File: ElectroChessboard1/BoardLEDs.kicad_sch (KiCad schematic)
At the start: 35 parts, among them IC73 CD74HC154M96

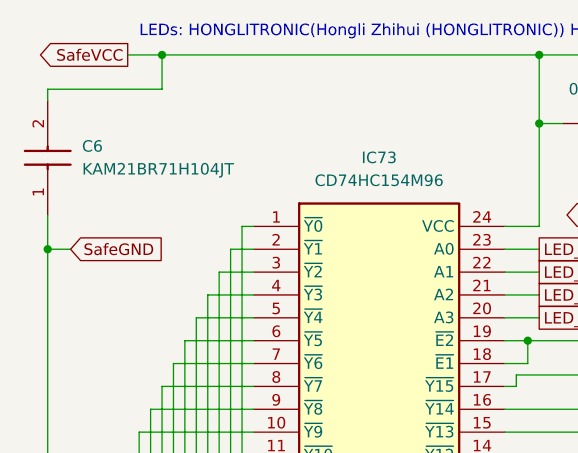
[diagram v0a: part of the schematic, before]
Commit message: Corrected footprints 1
Chosen footprints for JLCPCB
I may add USB insterface chip
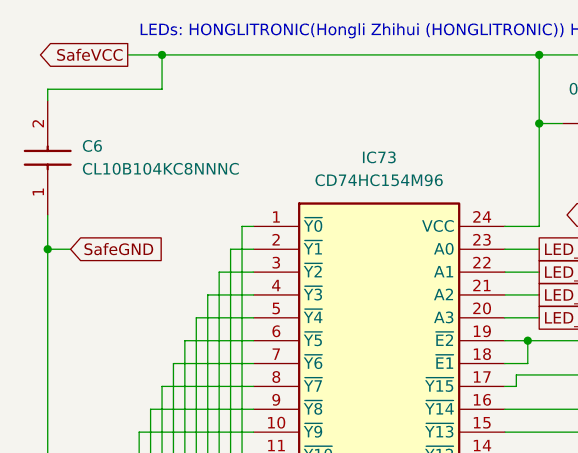
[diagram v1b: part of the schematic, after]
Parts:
- removed C6: KAM21BR71H104JT, CAPC2012X94N, symbol SamacSys_Parts:KAM21BR71H104JT
- added C6: CL10B104KC8NNNC, SamacSys_Parts:CAPC1608X90N, symbol SamacSys_Parts:CL10B104KC8NNNC
- IC73: footprint SOIC127P1030X265-24N -> SamacSys_Parts:SOIC127P1030X265-24N
- R10, R11, R12, R13, R14, R15, R16, R17, R18, R19, R2, R4, R5, R6, R7, R8, R9: footprint RESC1005X40N -> SamacSys_Parts:RESC1005X40N
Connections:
- net SafeGND: now also C6.1
- net SafeVCC: now also C6.2
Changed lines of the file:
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@@
 			)
 		)
-		(property "Footprint" "RESC1005X40N"
+		(property "Footprint" "SamacSys_Parts:RESC1005X40N"
 			(at 104.14 285.42 0)
 			(effects
@@
 			)
 		)
-		(property "Footprint" "RESC1005X40N"
+		(property "Footprint" "SamacSys_Parts:RESC1005X40N"
 			(at 104.14 193.98 0)
 			(effects
@@
 			)
 		)
-		(property "Footprint" "RESC1005X40N"
+		(property "Footprint" "SamacSys_Parts:RESC1005X40N"
 			(at 104.14 248.59 0)
 			(effects
@@
 			)
 		)
-		(property "Footprint" "RESC1005X40N"
+		(property "Footprint" "SamacSys_Parts:RESC1005X40N"
 			(at 104.14 166.04 0)
 			(effects
@@
 			)
 		)
-		(property "Footprint" "RESC1005X40N"
+		(property "Footprint" "SamacSys_Parts:RESC1005X40N"
 			(at 104.14 202.87 0)
 			(effects
@@
 	)
 	(symbol
+		(lib_id "SamacSys_Parts:CL10B104KC8NNNC")
+		(at 16.51 34.29 90)
+		(unit 1)
+		(exclude_from_sim no)
+		(in_bom yes)
+		(on_board yes)
+		(dnp no)
+		(fields_autoplaced yes)
+		(property "Reference" "C6"
+			(at 20.32 26.6699 90)
+			(effects
+				(font
+					(size 1.27 1.27)
+				)
+				(justify right)
+			)
+		)
+		(property "Value" "CL10B104KC8NNNC"
+			(at 20.32 29.2099 90)
+			(effects
+				(font
+					(size 1.27 1.27)
+				)
+				(justify right)
+			)
+		)
+		(property "Footprint" "SamacSys_Parts:CAPC1608X90N"
+			(at 112.7 25.4 0)
+			(effects
+				(font
+					(size 1.27 1.27)
+				)
+				(justify left top)
+				(hide yes)
+			)
+		)
+		(property "Datasheet" "https://datasheet.datasheetarchive.com/originals/distributors/DKDS-19/373511.pdf"
+			(at 212.7 25.4 0)
+			(effects
+				(font
+					(size 1.27 1.27)
+				)
+				(justify left top)
+				(hide yes)
+			)
+		)
+		(property "Description" "Samsung"
+			(at 16.51 34.29 0)
+			(effects
+				(font
+					(size 1.27 1.27)
+				)
+				(hide yes)
+			)
+		)
+		(property "Height" "0.9"
+			(at 412.7 25.4 0)
+			(effects
+				(font
+					(size 1.27 1.27)
+				)
+				(justify left top)
+				(hide yes)
+			)
+		)
+		(property "Mouser Part Number" "187-CL10B104KC8NNNC"
+			(at 512.7 25.4 0)
+			(effects
+				(font
+					(size 1.27 1.27)
+				)
+				(justify left top)
+				(hide yes)
+			)
+		)
+		(property "Mouser Price/Stock" "https://www.mouser.co.uk/ProductDetail/Samsung-Electro-Mechanics/CL10B104KC8NNNC?qs=%2FukktrhNKsY5bKXvqblW4Q%3D%3D"
+			(at 612.7 25.4 0)
+			(effects
+				(font
+					(size 1.27 1.27)
+				)
+				(justify left top)
+				(hide yes)
+			)
+		)
+		(property "Manufacturer_Name" "SAMSUNG"
+			(at 712.7 25.4 0)
+			(effects
+				(font
+					(size 1.27 1.27)
+				)
+				(justify left top)
+				(hide yes)
+			)
+		)
+		(property "Manufacturer_Part_Number" "CL10B104KC8NNNC"
+			(at 812.7 25.4 0)
+			(effects
+				(font
+					(size 1.27 1.27)
+				)
+				(justify left top)
+				(hide yes)
+			)
+		)
+		(pin "2"
+		)
+		(pin "1"
+		)
+		(instances
+			(project "ElectroChessboard1"
+				(path "/b40c7e57-cfb3-41c6-81be-f22d082b0927/7327273e-7754-4727-8b52-bb7f62babc74"
+					(reference "C6")
+					(unit 1)
+				)
+			)
+		)
+	)
+	(symbol
 		(lib_id "Device:LED")
 		(at 83.82 143.51 0)
@@
 			)
 		)
-		(property "Footprint" "RESC1005X40N"
+		(property "Footprint" "SamacSys_Parts:RESC1005X40N"
 			(at 104.14 185.09 0)
 			(effects
@@
 			)
 		)
-		(property "Footprint" "SOIC127P1030X265-24N"
+		(property "Footprint" "SamacSys_Parts:SOIC127P1030X265-24N"
 			(at 63.5 130.48 0)
 			(effects
@@
 			)
 		)
-		(property "Footprint" "RESC1005X40N"
+		(property "Footprint" "SamacSys_Parts:RESC1005X40N"
 			(at 104.14 258.75 0)
 			(effects
@@
 			)
 		)
-		(property "Footprint" "RESC1005X40N"
+		(property "Footprint" "SamacSys_Parts:RESC1005X40N"
 			(at 104.14 239.7 0)
 			(effects
@@
 			)
 		)
-		(property "Footprint" "RESC1005X40N"
+		(property "Footprint" "SamacSys_Parts:RESC1005X40N"
 			(at 104.14 276.53 0)
 			(effects
@@
 			)
 		)
-		(property "Footprint" "RESC1005X40N"
+		(property "Footprint" "SamacSys_Parts:RESC1005X40N"
 			(at 104.14 211.76 0)
 			(effects
@@
 			)
 		)
-		(property "Footprint" "RESC1005X40N"
+		(property "Footprint" "SamacSys_Parts:RESC1005X40N"
 			(at 104.14 221.92 0)
 			(effects
@@
 			)
 		)
-		(property "Footprint" "RESC1005X40N"
+		(property "Footprint" "SamacSys_Parts:RESC1005X40N"
 			(at 104.14 230.81 0)
 			(effects
@@
 			)
 		)
-		(property "Footprint" "RESC1005X40N"
+		(property "Footprint" "SamacSys_Parts:RESC1005X40N"
 			(at 104.14 157.15 0)
 			(effects
@@
 			)
 		)
-		(property "Footprint" "RESC1005X40N"
+		(property "Footprint" "SamacSys_Parts:RESC1005X40N"
 			(at 104.14 267.64 0)
 			(effects
@@
 			)
 		)
-		(property "Footprint" "RESC1005X40N"
+		(property "Footprint" "SamacSys_Parts:RESC1005X40N"
 			(at 104.14 174.93 0)
 			(effects
@@
 	)
 	(symbol
-		(lib_id "SamacSys_Parts:KAM21BR71H104JT")
-		(at 16.51 34.29 90)
-		(unit 1)
-		(exclude_from_sim no)
-		(in_bom yes)
-		(on_board yes)
-		(dnp no)
-		(fields_autoplaced yes)
-		(property "Reference" "C6"
-			(at 20.32 26.6699 90)
-			(effects
-				(font
-					(size 1.27 1.27)
-				)
-				(justify right)
-			)
-		)
-		(property "Value" "KAM21BR71H104JT"
-			(at 20.32 29.2099 90)
-			(effects
-				(font
-					(size 1.27 1.27)
-				)
-				(justify right)
-			)
-		)
-		(property "Footprint" "CAPC2012X94N"
-			(at 112.7 25.4 0)
-			(effects
-				(font
-					(size 1.27 1.27)
-				)
-				(justify left top)
-				(hide yes)
-			)
-		)
-		(property "Datasheet" "https://spicat.kyocera-avx.com/product/mlcc/chartview/KAM21BR71H104JT/DataSheet/X7R"
-			(at 212.7 25.4 0)
-			(effects
-				(font
-					(size 1.27 1.27)
-				)
-				(justify left top)
-				(hide yes)
-			)
-		)
-		(property "Description" "Multilayer Ceramic Capacitors MLCC - SMD/SMT 50V .1uF X7R 0805 5% AEC-Q200"
-			(at 16.51 34.29 0)
-			(effects
-				(font
-					(size 1.27 1.27)
-				)
-				(hide yes)
-			)
-		)
-		(property "Height" "0.94"
-			(at 412.7 25.4 0)
-			(effects
-				(font
-					(size 1.27 1.27)
-				)
-				(justify left top)
-				(hide yes)
-			)
-		)
-		(property "Mouser Part Number" "581-KAM21BR71H104JT"
-			(at 512.7 25.4 0)
-			(effects
-				(font
-					(size 1.27 1.27)
-				)
-				(justify left top)
-				(hide yes)
-			)
-		)
-		(property "Mouser Price/Stock" "https://www.mouser.co.uk/ProductDetail/KYOCERA-AVX/KAM21BR71H104JT?qs=Jm2GQyTW%2Fbic6Zk4McEt6w%3D%3D"
-			(at 612.7 25.4 0)
-			(effects
-				(font
-					(size 1.27 1.27)
-				)
-				(justify left top)
-				(hide yes)
-			)
-		)
-		(property "Manufacturer_Name" "Kyocera AVX"
-			(at 712.7 25.4 0)
-			(effects
-				(font
-					(size 1.27 1.27)
-				)
-				(justify left top)
-				(hide yes)
-			)
-		)
-		(property "Manufacturer_Part_Number" "KAM21BR71H104JT"
-			(at 812.7 25.4 0)
-			(effects
-				(font
-					(size 1.27 1.27)
-				)
-				(justify left top)
-				(hide yes)
-			)
-		)
-		(pin "1"
-		)
-		(pin "2"
-		)
-		(instances
-			(project "ElectroChessboard1"
-				(path "/b40c7e57-cfb3-41c6-81be-f22d082b0927/7327273e-7754-4727-8b52-bb7f62babc74"
-					(reference "C6")
-					(unit 1)
-				)
-			)
-		)
-	)
-	(symbol
 		(lib_id "SamacSys_Parts:0402WGF1002TCE")
 		(at 73.66 24.13 0)
@@
 			)
 		)
-		(property "Footprint" "RESC1005X40N"
+		(property "Footprint" "SamacSys_Parts:RESC1005X40N"
 			(at 87.63 120.32 0)
 			(effects
@@
 			)
 		)
-		(property "Footprint" "RESC1005X40N"
+		(property "Footprint" "SamacSys_Parts:RESC1005X40N"
 			(at 104.14 148.26 0)
 			(effects
